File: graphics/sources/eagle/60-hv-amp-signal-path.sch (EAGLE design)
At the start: 43 parts, among them X1 IN, X13 MON+, X14 MON-, X5 HV_IN+, X6 HV_IN-

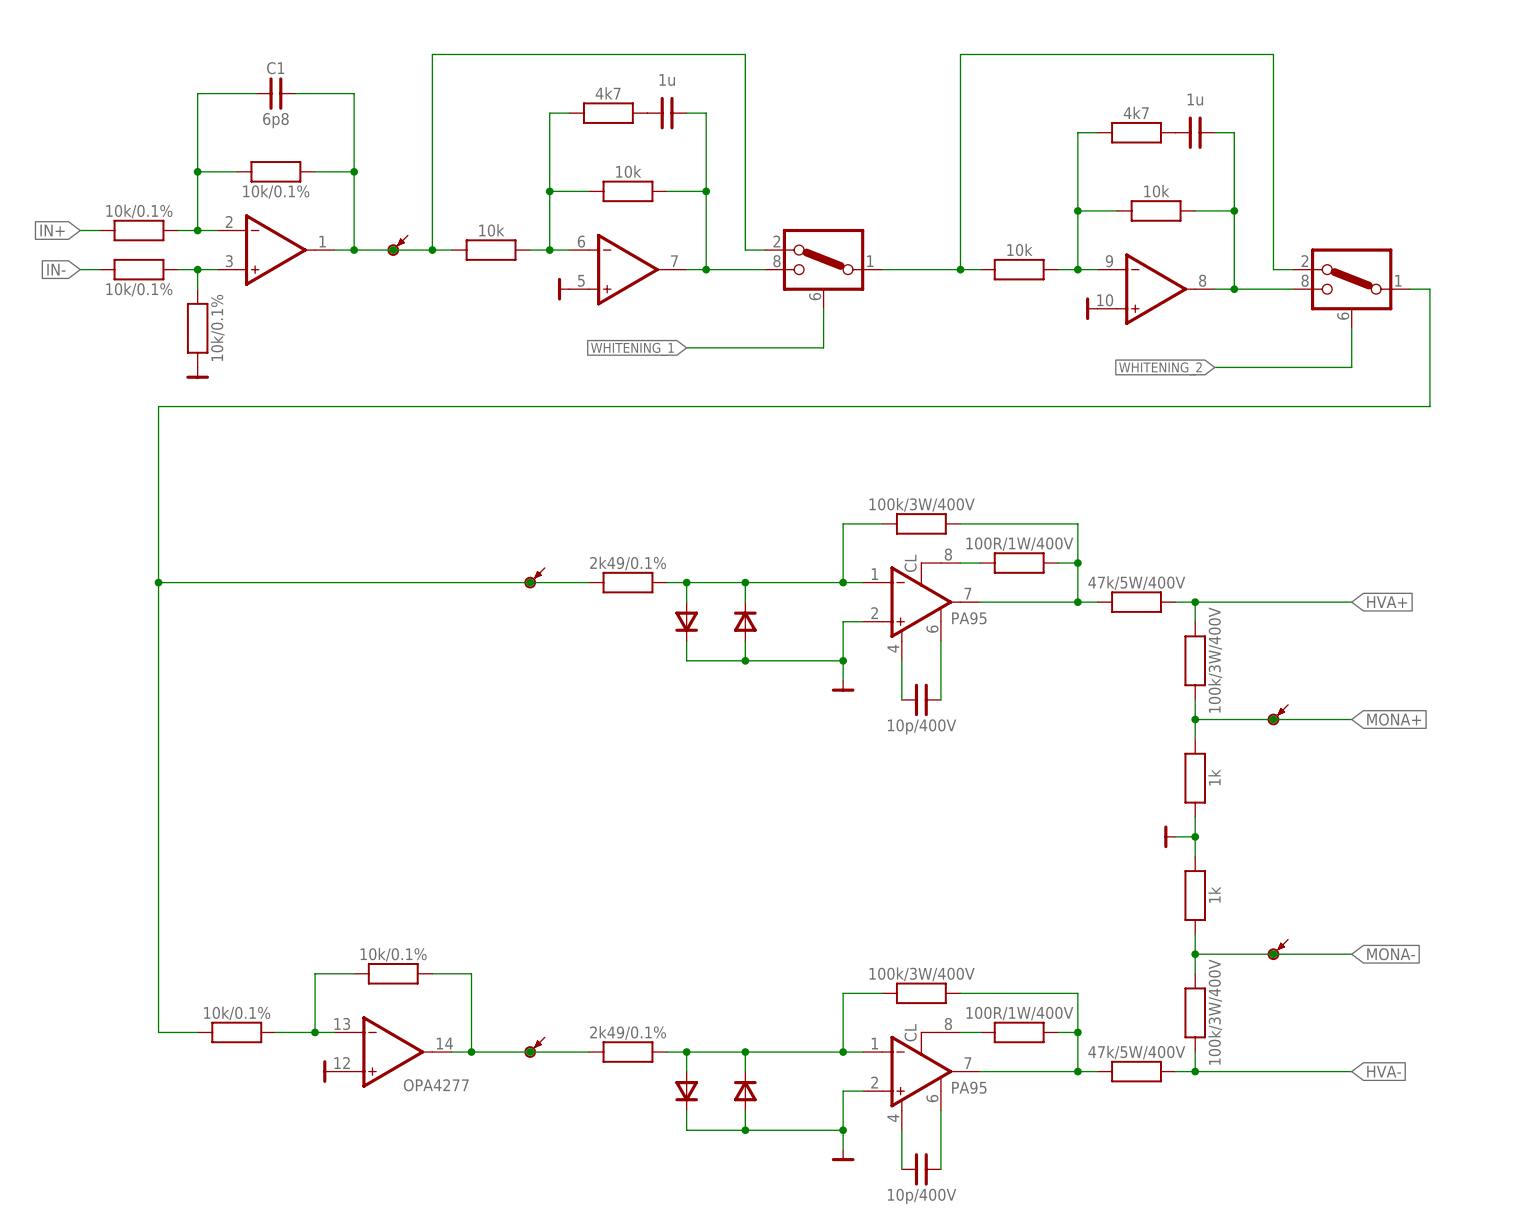
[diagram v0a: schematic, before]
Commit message: Added annotations to Eagle diagrams. Still needs textual updates.
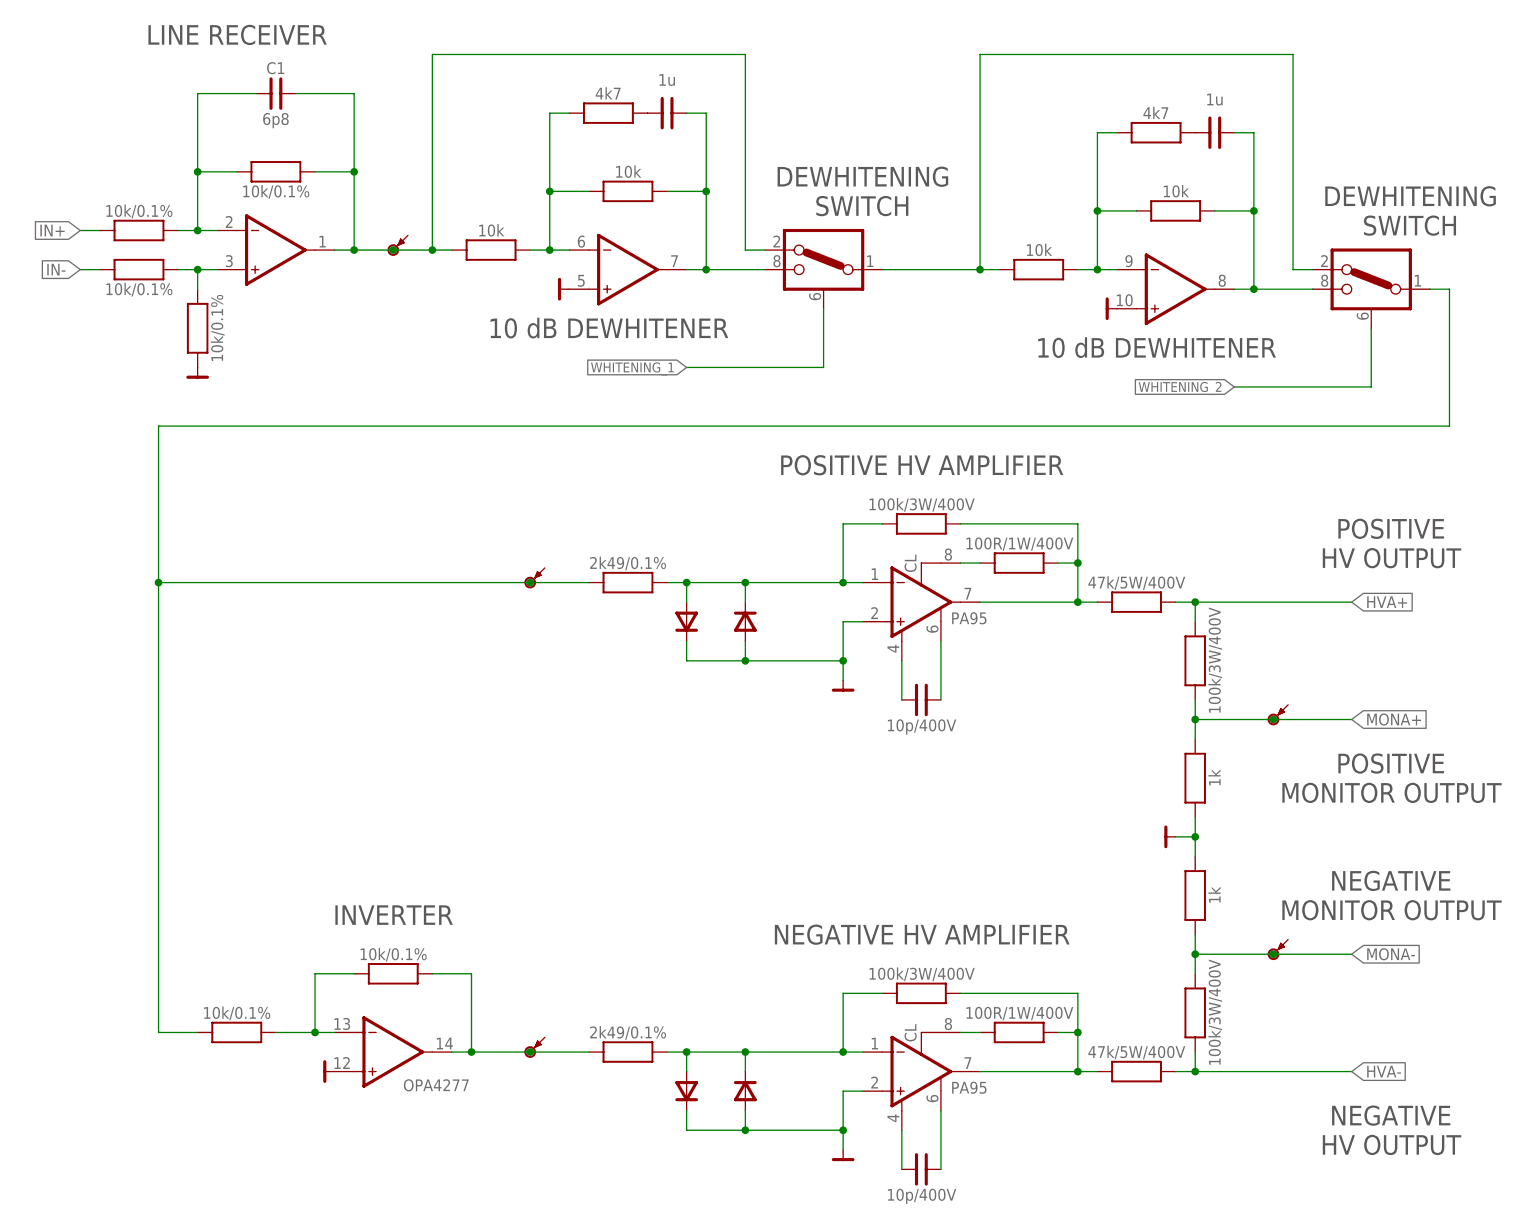
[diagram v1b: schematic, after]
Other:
- note added: "10 dB DEWHITENER"
- note added: "DEWHITENING SWITCH"
- note added: "INVERTER"
- note added: "LINE RECEIVER"
- note added: "NEGATIVE HV AMPLIFIER"
- note added: "NEGATIVE HV OUTPUT"
- note added: "NEGATIVE MONITOR OUTPUT"
- note added: "POSITIVE HV AMPLIFIER"
- note added: "POSITIVE HV OUTPUT"
- note added: "POSITIVE MONITOR OUTPUT"
